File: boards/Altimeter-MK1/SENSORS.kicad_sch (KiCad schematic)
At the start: 14 parts, among them U1 LSM9DS1, U2 MS5611-01BA, U3 H3LIS331DL

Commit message: Trello not working/mcu sensor connections (#119)
* connected ejection/sensors sheets to mcu

* added gps module to sensor sheet and repositioned boxes (#115)

Co-authored-by: Eisha Peyyeti <eisha.peyyeti@gmail.com>

* deleted GPS kicad_sch

* Av 685/altimeter mcu schematic (#116)

* added jtag connector and fixed power supply

* added memory chip to schematic

* Update MCU.kicad_sch

* Update MCU.kicad_sch

* Update MCU.kicad_sch

* Delete #auto_saved_files#

* Update MCU.kicad_sch

* formatting changes

* kicad changes

* Changes in MCU and SENSORS

NEVER USE SENSORS BRANCH EVER AGAIN LOL

* removed auto saved files

* Update MCU.kicad_sch

* finished mcu schematic

* Added Ematch sensing

* Organized MCU and added CubeMX File

* added notes on unused nand flash signals

* changed buzzer pwm net name to be all caps

* added usb type c receptacle, and esd protection, to schematic

* added test points

* mcu cleanup

* 8/11 Changes

Connected GPS and HopeFM module. Added voltage sensing

Co-authored-by: Arna Bhardwaj <arnabhardwaj@Arnas-MacBook-Air.local>
Co-authored-by: TurtlePhuchka <richeek2@illinois.edu>
Co-authored-by: Peter Giannetos <pg19@illinois.edu>
Co-authored-by: Eisha Peyyeti <eisha.peyyeti@gmail.com>
Co-authored-by: navyasm <108916984+navyasm@users.noreply.github.com>
Co-authored-by: JayBeeRose <109769325+JayBeeRose@users.noreply.github.com>

Co-authored-by: Arna Bhardwaj <arnabhardwaj@Arnas-MacBook-Air.local>
Co-authored-by: Eisha Peyyeti <eisha.peyyeti@gmail.com>
Co-authored-by: TurtlePhuchka <richeek2@illinois.edu>
Co-authored-by: Peter Giannetos <pg19@illinois.edu>
Co-authored-by: navyasm <108916984+navyasm@users.noreply.github.com>
Co-authored-by: JayBeeRose <109769325+JayBeeRose@users.noreply.github.com>
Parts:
- added U?: ~, symbol RF_GPS:SAM-M8Q
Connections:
- net GND: now also U?.1 (GND), U?.10 (GND), U?.11 (GND), U?.15 (GND), U?.16 (GND), U?.20 (GND), U?.4 (GND), U?.5 (GND), U?.6 (GND)
- new net SAM-M8Q_EXTINT: U?.19 (EXTINT)
- new net SAM-M8Q_SCL: U?.12 (SCL)
- new net SAM-M8Q_SDA: U?.9 (SDA)
- new net VBUS: U?.17 (VCC), U?.2 (VCC_IO), U?.3 (V_BCKP)
- no-connect marks 0 -> 5
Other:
- note added: "SAM-M8Q"
- note added: "Should some of these flags be designated as something other than just an input? (Input, Output, Both, etc.)"
- company: (none) -> The Illinois Space Society
- title: (none) -> Altimeter Sensors Schematic Mk1
- moved on the sheet: C1, C2, C3, C4, C5, C6, C7, C8, JP1, JP2, JP3, U1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

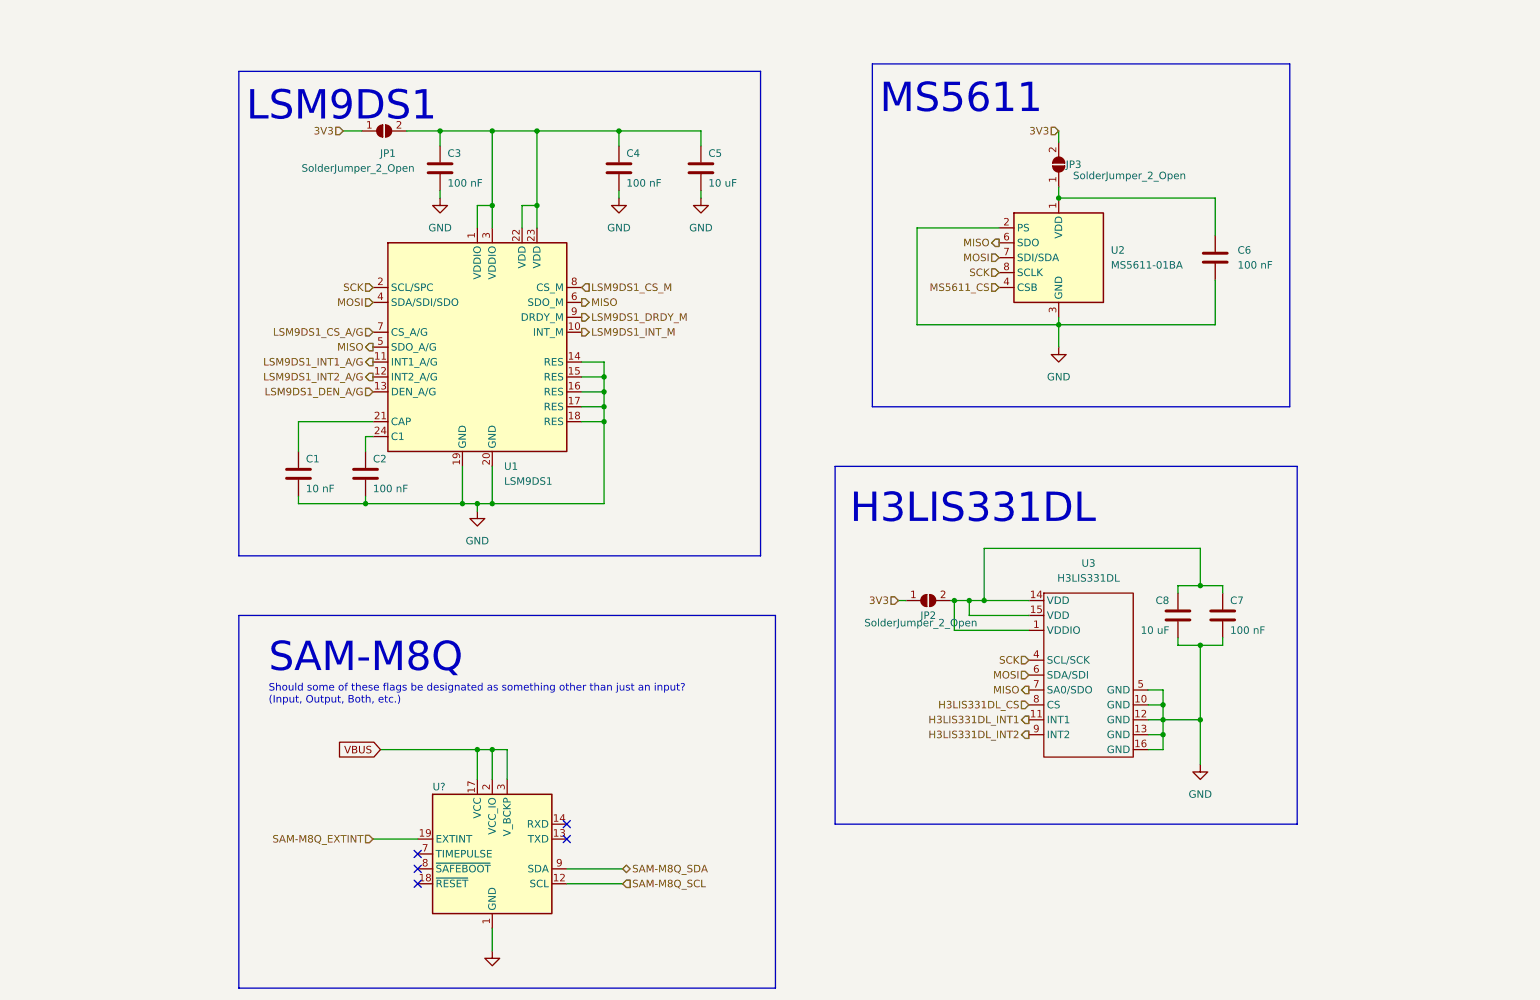
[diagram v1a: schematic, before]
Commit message: REBBASE BRANCHES - Worked on b2b connections
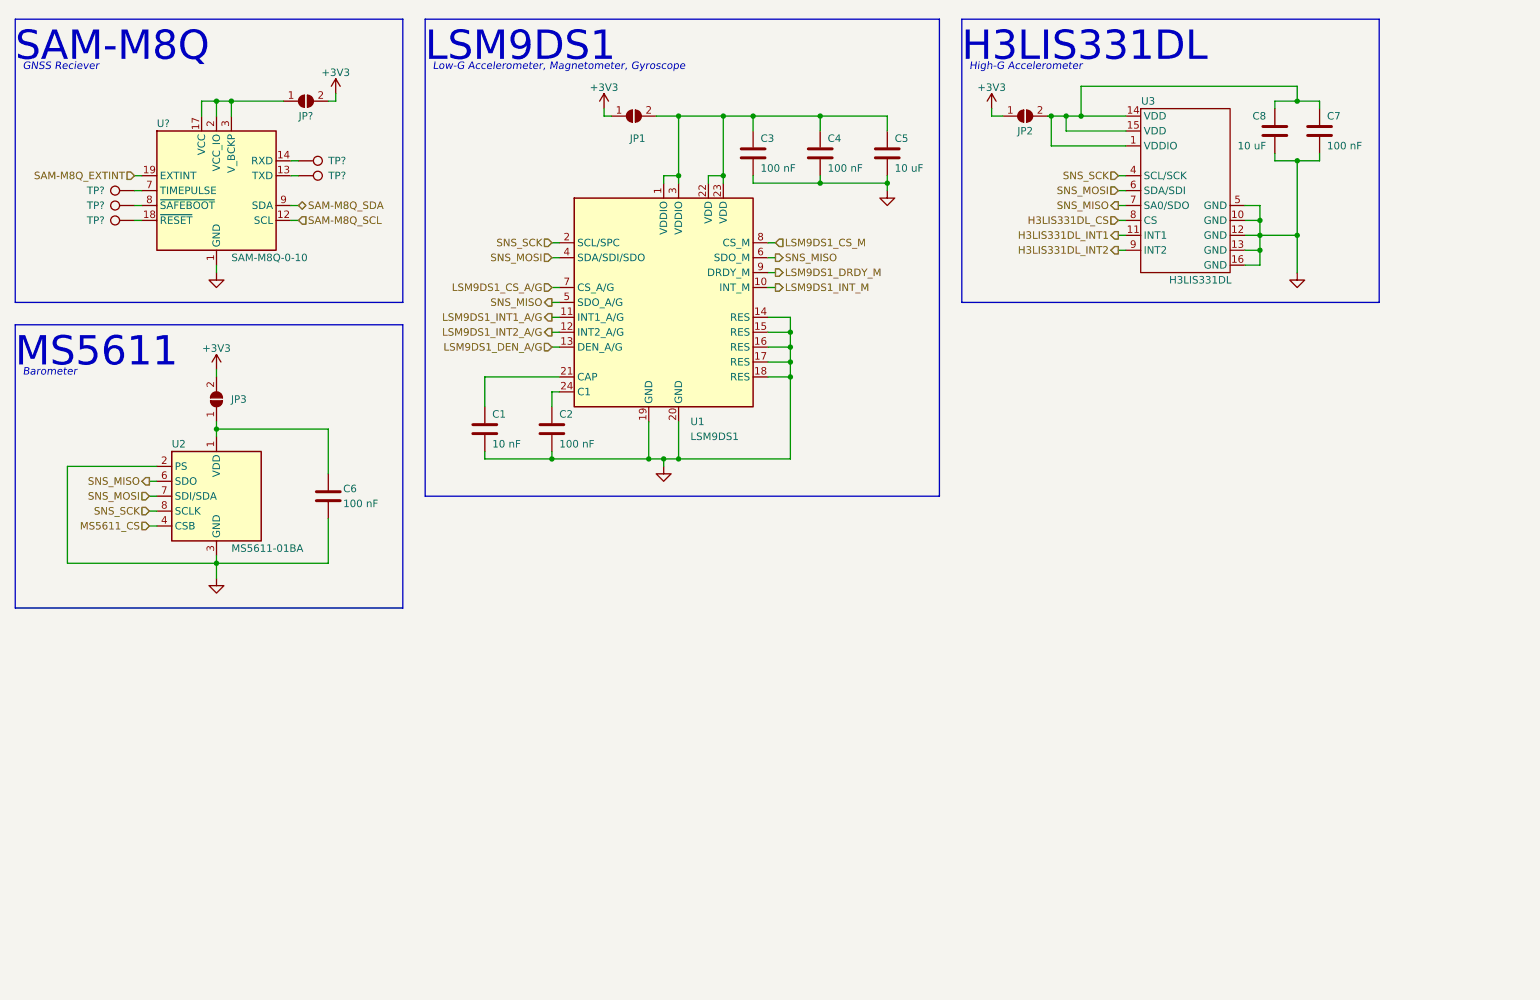
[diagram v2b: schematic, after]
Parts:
- added JP?: SolderJumper_2_Open, Jumper:SolderJumper-2_P1.3mm_Open_RoundedPad1.0x1.5mm, symbol Jumper:SolderJumper_2_Open
- added TP? (x5): TestPoint, symbol Connector:TestPoint
- U?: value ~ -> SAM-M8Q-0-10
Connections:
- net at U?.13 (TXD): now also TP?.1
- net at U?.14 (RXD): now also TP?.1
- net at U?.18 (~{RESET}): now also TP?.1
- net at U?.7 (TIMEPULSE): now also TP?.1
- net at U?.8 (~{SAFEBOOT}): now also TP?.1
- net 3V3 renamed +3V3
- net +3V3: now also JP?.2 (B)
- net MISO renamed SNS_MISO
- net MOSI renamed SNS_MOSI
- net SCK renamed SNS_SCK
- net VBUS: no longer names the net of U?.17 (VCC), U?.2 (VCC_IO), U?.3 (V_BCKP)
- net VBUS: now also JP?.1 (A)
- no-connect marks 5 -> 0
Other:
- note added: "Barometer"
- note added: "GNSS Reciever"
- note added: "High-G Accelerometer"
- note added: "Low-G Accelerometer, Magnetometer, Gyroscope"
- note removed: "Should some of these flags be designated as something other than just an input? (Input, Output, Both, etc.)"
- moved on the sheet: C1, C2, C3, C4, C5, C6, C7, C8, JP1, JP2, JP3, U1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

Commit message: Annoted full schematic 8/12
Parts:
- gave numbers to parts that had none: 7
- renumbered C6 to C301, C1 to C302, C2 to C303, C3 to C304, C4 to C305, C5 to C306, C8 to C307, C7 to C308, JP3 to JP301, JP1 to JP303, JP2 to JP304, U2 to U302, U1 to U303, U3 to U304
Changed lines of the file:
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@@
   (symbol (lib_id "Device:C") (at 237.49 34.29 0) (unit 1)
     (in_bom yes) (on_board yes)
-    (property "Reference" "C7" (id 0) (at 238.76 31.75 0)
+    (property "Reference" "C308" (id 0) (at 238.76 31.75 0)
       (effects (font (size 1.27 1.27)) (justify left))
     )
@@
   (symbol (lib_id "power:+3V3") (at 69.85 27.94 0) (unit 1)
     (in_bom yes) (on_board yes) (fields_autoplaced)
-    (property "Reference" "#PWR?" (id 0) (at 69.85 31.75 0)
+    (property "Reference" "#PWR0304" (id 0) (at 69.85 31.75 0)
       (effects (font (size 1.27 1.27)) hide)
     )
@@
   (symbol (lib_id "power:+3V3") (at 181.61 30.48 0) (unit 1)
     (in_bom yes) (on_board yes) (fields_autoplaced)
-    (property "Reference" "#PWR?" (id 0) (at 181.61 34.29 0)
+    (property "Reference" "#PWR0308" (id 0) (at 181.61 34.29 0)
       (effects (font (size 1.27 1.27)) hide)
     )
@@
   (symbol (lib_id "Jumper:SolderJumper_2_Open") (at 187.325 31.75 0) (unit 1)
     (in_bom yes) (on_board yes)
-    (property "Reference" "JP2" (id 0) (at 187.325 34.29 0))
+    (property "Reference" "JP304" (id 0) (at 187.325 34.29 0))
     (property "Value" "SolderJumper_2_Open" (id 1) (at 186.055 35.56 0)
       (effects (font (size 1.27 1.27)) hide)
@@
   (symbol (lib_id "power:GND") (at 49.53 58.42 0) (unit 1)
     (in_bom yes) (on_board yes) (fields_autoplaced)
-    (property "Reference" "#PWR?" (id 0) (at 49.53 64.77 0)
+    (property "Reference" "#PWR0301" (id 0) (at 49.53 64.77 0)
       (effects (font (size 1.27 1.27)) hide)
     )
@@
   (symbol (lib_id "Device:C") (at 163.83 38.1 0) (unit 1)
     (in_bom yes) (on_board yes)
-    (property "Reference" "C5" (id 0) (at 165.1 35.56 0)
+    (property "Reference" "C306" (id 0) (at 165.1 35.56 0)
       (effects (font (size 1.27 1.27)) (justify left))
     )
@@
   (symbol (lib_id "power:+3V3") (at 115.57 30.48 0) (unit 1)
     (in_bom yes) (on_board yes) (fields_autoplaced)
-    (property "Reference" "#PWR?" (id 0) (at 115.57 34.29 0)
+    (property "Reference" "#PWR0305" (id 0) (at 115.57 34.29 0)
       (effects (font (size 1.27 1.27)) hide)
     )
@@
   (symbol (lib_id "Connector:TestPoint") (at 35.56 49.53 90) (unit 1)
     (in_bom yes) (on_board yes)
-    (property "Reference" "TP?" (id 0) (at 30.48 49.53 90)
+    (property "Reference" "TP303" (id 0) (at 30.48 49.53 90)
       (effects (font (size 1.27 1.27)) (justify left))
     )
@@
   (symbol (lib_id "Connector:TestPoint") (at 35.56 44.45 90) (unit 1)
     (in_bom yes) (on_board yes)
-    (property "Reference" "TP?" (id 0) (at 30.48 44.45 90)
+    (property "Reference" "TP301" (id 0) (at 30.48 44.45 90)
       (effects (font (size 1.27 1.27)) (justify left))
     )
@@
   (symbol (lib_id "Connector:TestPoint") (at 35.56 46.99 90) (unit 1)
     (in_bom yes) (on_board yes)
-    (property "Reference" "TP?" (id 0) (at 30.48 46.99 90)
+    (property "Reference" "TP302" (id 0) (at 30.48 46.99 90)
       (effects (font (size 1.27 1.27)) (justify left))
     )
@@
   (symbol (lib_id "Device:C") (at 152.4 38.1 0) (unit 1)
     (in_bom yes) (on_board yes)
-    (property "Reference" "C4" (id 0) (at 153.67 35.56 0)
+    (property "Reference" "C305" (id 0) (at 153.67 35.56 0)
       (effects (font (size 1.27 1.27)) (justify left))
     )
@@
   (symbol (lib_id "Device:C") (at 140.97 38.1 0) (unit 1)
     (in_bom yes) (on_board yes)
-    (property "Reference" "C3" (id 0) (at 142.24 35.56 0)
+    (property "Reference" "C304" (id 0) (at 142.24 35.56 0)
       (effects (font (size 1.27 1.27)) (justify left))
     )
@@
   (symbol (lib_id "power:GND") (at 125.73 91.44 0) (unit 1)
     (in_bom yes) (on_board yes) (fields_autoplaced)
-    (property "Reference" "#PWR?" (id 0) (at 125.73 97.79 0)
+    (property "Reference" "#PWR0306" (id 0) (at 125.73 97.79 0)
       (effects (font (size 1.27 1.27)) hide)
     )
@@
   (symbol (lib_id "power:GND") (at 163.83 44.45 0) (unit 1)
     (in_bom yes) (on_board yes) (fields_autoplaced)
-    (property "Reference" "#PWR?" (id 0) (at 163.83 50.8 0)
+    (property "Reference" "#PWR0307" (id 0) (at 163.83 50.8 0)
       (effects (font (size 1.27 1.27)) hide)
     )
@@
   (symbol (lib_id "H3LIS331DL:H3LIS331DL") (at 214.63 45.72 0) (unit 1)
     (in_bom yes) (on_board yes)
-    (property "Reference" "U3" (id 0) (at 208.28 29.21 0))
+    (property "Reference" "U304" (id 0) (at 208.28 29.21 0))
     (property "Value" "H3LIS331DL" (id 1) (at 217.17 59.69 0))
     (property "Footprint" "Package_LGA:LGA-16_3x3mm_P0.5mm_LayoutBorder3x5y" (id 2) (at 214.63 62.23 0)
@@
   (symbol (lib_id "Jumper:SolderJumper_2_Open") (at 64.77 29.21 0) (unit 1)
     (in_bom yes) (on_board yes)
-    (property "Reference" "JP?" (id 0) (at 64.77 31.75 0))
+    (property "Reference" "JP302" (id 0) (at 64.77 31.75 0))
     (property "Value" "SolderJumper_2_Open" (id 1) (at 63.5 33.02 0)
       (effects (font (size 1.27 1.27)) hide)
@@
   (symbol (lib_id "Jumper:SolderJumper_2_Open") (at 49.53 80.01 90) (unit 1)
     (in_bom yes) (on_board yes)
-    (property "Reference" "JP3" (id 0) (at 53.34 80.01 90))
+    (property "Reference" "JP301" (id 0) (at 53.34 80.01 90))
     (property "Value" "SolderJumper_2_Open" (id 1) (at 61.595 81.915 90)
       (effects (font (size 1.27 1.27)) hide)
@@
   (symbol (lib_id "power:GND") (at 49.53 110.49 0) (unit 1)
     (in_bom yes) (on_board yes) (fields_autoplaced)
-    (property "Reference" "#PWR?" (id 0) (at 49.53 116.84 0)
+    (property "Reference" "#PWR0303" (id 0) (at 49.53 116.84 0)
       (effects (font (size 1.27 1.27)) hide)
     )
@@
   (symbol (lib_id "Sensor_Motion:LSM9DS1") (at 125.73 63.5 0) (unit 1)
     (in_bom yes) (on_board yes) (fields_autoplaced)
-    (property "Reference" "U1" (id 0) (at 130.2894 83.82 0)
+    (property "Reference" "U303" (id 0) (at 130.2894 83.82 0)
       (effects (font (size 1.27 1.27)) (justify left))
     )
@@
   (symbol (lib_id "power:GND") (at 233.68 58.42 0) (unit 1)
     (in_bom yes) (on_board yes) (fields_autoplaced)
-    (property "Reference" "#PWR?" (id 0) (at 233.68 64.77 0)
+    (property "Reference" "#PWR0309" (id 0) (at 233.68 64.77 0)
       (effects (font (size 1.27 1.27)) hide)
     )
@@
   (symbol (lib_id "Connector:TestPoint") (at 63.5 41.91 270) (unit 1)
     (in_bom yes) (on_board yes)
-    (property "Reference" "TP?" (id 0) (at 68.58 41.91 90)
+    (property "Reference" "TP305" (id 0) (at 68.58 41.91 90)
       (effects (font (size 1.27 1.27)) (justify left))
     )
@@
   (symbol (lib_id "Sensor_Pressure:MS5611-01BA") (at 49.53 96.52 0) (unit 1)
     (in_bom yes) (on_board yes)
-    (property "Reference" "U2" (id 0) (at 41.91 87.63 0)
+    (property "Reference" "U302" (id 0) (at 41.91 87.63 0)
       (effects (font (size 1.27 1.27)) (justify left))
     )
@@
   (symbol (lib_id "RF_GPS:SAM-M8Q") (at 49.53 44.45 0) (unit 1)
     (in_bom yes) (on_board yes)
-    (property "Reference" "U?" (id 0) (at 39.37 33.02 0)
+    (property "Reference" "U301" (id 0) (at 39.37 33.02 0)
       (effects (font (size 1.27 1.27)) (justify left))
     )
@@
   (symbol (lib_id "power:+3V3") (at 49.53 74.93 0) (unit 1)
     (in_bom yes) (on_board yes) (fields_autoplaced)
-    (property "Reference" "#PWR?" (id 0) (at 49.53 78.74 0)
+    (property "Reference" "#PWR0302" (id 0) (at 49.53 78.74 0)
       (effects (font (size 1.27 1.27)) hide)
     )
@@
   (symbol (lib_id "Device:C") (at 229.87 34.29 0) (unit 1)
     (in_bom yes) (on_board yes)
-    (property "Reference" "C8" (id 0) (at 226.06 31.75 0)
+    (property "Reference" "C307" (id 0) (at 226.06 31.75 0)
       (effects (font (size 1.27 1.27)) (justify left))
     )
@@
   (symbol (lib_id "Jumper:SolderJumper_2_Open") (at 120.65 31.75 0) (unit 1)
     (in_bom yes) (on_board yes)
-    (property "Reference" "JP1" (id 0) (at 121.285 35.56 0))
+    (property "Reference" "JP303" (id 0) (at 121.285 35.56 0))
     (property "Value" "SolderJumper_2_Open" (id 1) (at 116.205 38.1 0)
       (effects (font (size 1.27 1.27)) hide)
@@
   (symbol (lib_id "Connector:TestPoint") (at 63.5 39.37 270) (unit 1)
     (in_bom yes) (on_board yes)
-    (property "Reference" "TP?" (id 0) (at 68.58 39.37 90)
+    (property "Reference" "TP304" (id 0) (at 68.58 39.37 90)
       (effects (font (size 1.27 1.27)) (justify left))
     )
@@
   (symbol (lib_id "Device:C") (at 106.68 85.09 0) (unit 1)
     (in_bom yes) (on_board yes)
-    (property "Reference" "C2" (id 0) (at 107.95 82.55 0)
+    (property "Reference" "C303" (id 0) (at 107.95 82.55 0)
       (effects (font (size 1.27 1.27)) (justify left))
     )
@@
   (symbol (lib_id "Device:C") (at 95.25 85.09 0) (unit 1)
     (in_bom yes) (on_board yes)
-    (property "Reference" "C1" (id 0) (at 96.52 82.55 0)
+    (property "Reference" "C302" (id 0) (at 96.52 82.55 0)
       (effects (font (size 1.27 1.27)) (justify left))
     )
@@
   (symbol (lib_id "Device:C") (at 68.58 96.52 0) (unit 1)
     (in_bom yes) (on_board yes)
-    (property "Reference" "C6" (id 0) (at 71.12 95.25 0)
-      (effects (font (size 1.27 1.27)) (justify left))
-    )
+    (property "Reference" "C301" (id 0) (at 71.12 95.25 0)
+      (effects (font (size 1.27 1.27)) (justify left))
+    )
